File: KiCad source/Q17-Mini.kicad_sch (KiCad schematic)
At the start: 80 parts, among them J1 Input, J2-1 SPK+, J2-2 SPK-, J3-1 V+, J3-2 GND, J3-3 V-, Q1 IRF610, Q10 KSA992, Q11 BS250P, Q12 BD139, Q13 IRF610, Q14 IRF9610, Q15 FQA46N15, Q16 FQA36P15, Q2 KSA992, Q3 KSC1845, Q4 IRF9610, Q5 FQP3P20, Q6 FQP3N30, Q7 KSC1845, Q8 ZVN4206AV, Q9 BS250P, U1 OPA1641

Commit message: PCB v1.0.8 FINAL
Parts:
- R11, R12: value 47R/1W -> 47R/2W
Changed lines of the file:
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@@
   (title_block
     (title "Q17-Mini Amplifier")
-    (date "2021-11-27")
+    (date "2021-11-28")
     (rev "1.0.8")
     (company "by eng. Tiberiu Vicol")
@@
       (effects (font (size 1.27 1.27)) (justify left))
     )
-    (property "Value" "47R/1W" (id 1) (at 180.5941 69.9833 0)
+    (property "Value" "47R/2W" (id 1) (at 180.5941 69.9833 0)
       (effects (font (size 1.27 1.27)) (justify left))
     )
@@
       (effects (font (size 1.27 1.27)) (justify left))
     )
-    (property "Value" "47R/1W" (id 1) (at 180.5941 102.2413 0)
+    (property "Value" "47R/2W" (id 1) (at 180.5941 102.2413 0)
       (effects (font (size 1.27 1.27)) (justify left))
     )
@@
     )
     (path "/15b91c78-18e1-4f64-926c-7e4784683c4f"
-      (reference "R11") (unit 1) (value "47R/1W") (footprint "Resistor_THT:R_Axial_DIN0411_L9.9mm_D3.6mm_P12.70mm_Horizontal")
+      (reference "R11") (unit 1) (value "47R/2W") (footprint "Resistor_THT:R_Axial_DIN0411_L9.9mm_D3.6mm_P12.70mm_Horizontal")
     )
     (path "/650c038f-de6c-4533-9f4a-887a91a93957"
-      (reference "R12") (unit 1) (value "47R/1W") (footprint "Resistor_THT:R_Axial_DIN0411_L9.9mm_D3.6mm_P12.70mm_Horizontal")
+      (reference "R12") (unit 1) (value "47R/2W") (footprint "Resistor_THT:R_Axial_DIN0411_L9.9mm_D3.6mm_P12.70mm_Horizontal")
     )
     (path "/02f26f68-bf34-47b8-a58c-12fbe031c778"

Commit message: Schematic v1.0.9
Some mods on text.
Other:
- note added: "R27 : Use good low noise 1W resistor (CMF60560R00JKR6)."
- note removed: "R27 : Use good low noise and low ppm 1W resistor."
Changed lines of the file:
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@@
   (title_block
     (title "Q17-Mini Amplifier")
-    (date "2021-11-28")
-    (rev "1.0.8")
+    (date "2021-11-29")
+    (rev "1.0.9")
     (company "by eng. Tiberiu Vicol")
     (comment 1 "Modified by Stef for the Q17-Mini project")
@@
     (effects (font (size 1.27 1.27)) (justify left bottom))
   )
-  (text "R27 : Use good low noise and low ppm 1W resistor." (at 93.98 177.8 0)
+  (text "R27 : Use good low noise 1W resistor (CMF60560R00JKR6)."
+    (at 93.98 177.8 0)
     (effects (font (size 1.27 1.27)) (justify left bottom))
   )

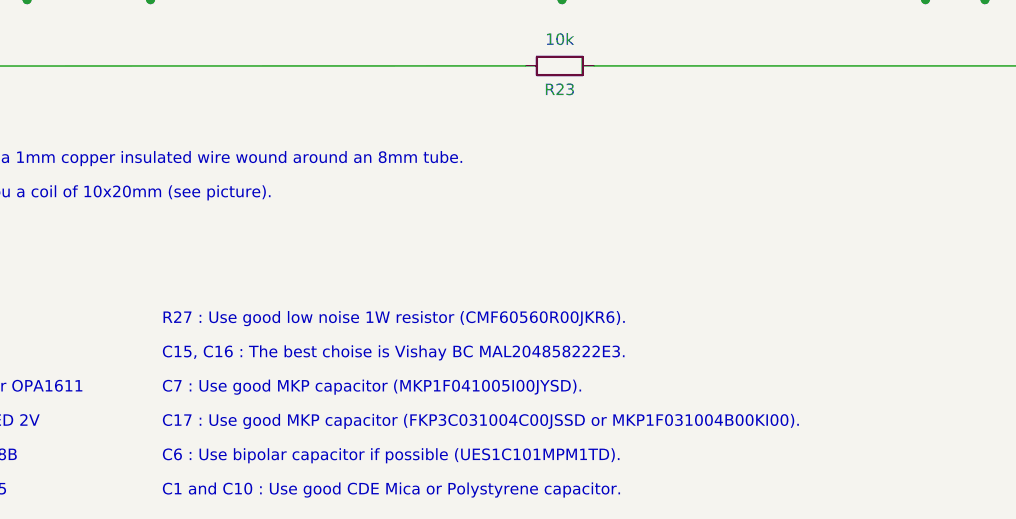
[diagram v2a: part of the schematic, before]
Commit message: Schematic v1.0.9
Some mods on comment text.
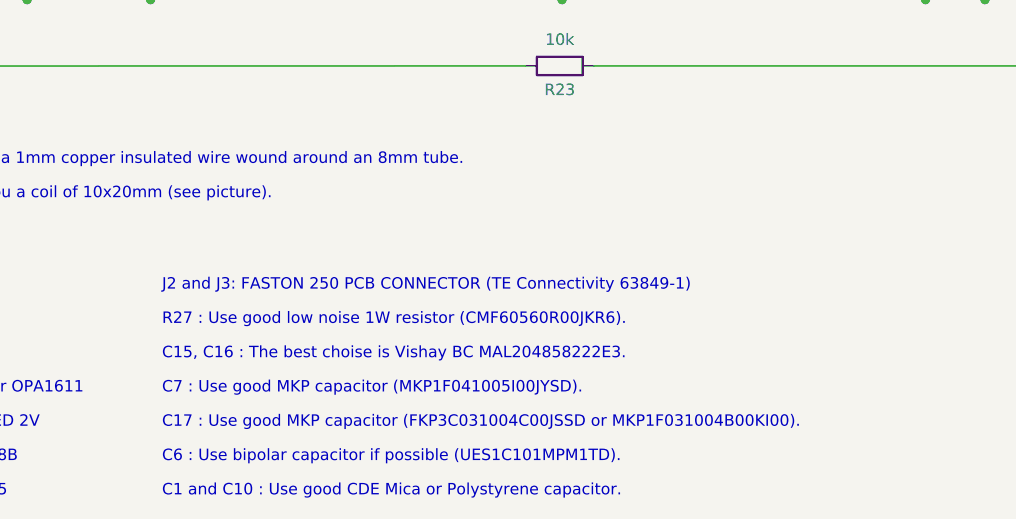
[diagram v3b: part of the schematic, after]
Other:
- note added: "J2 and J3: FASTON 250 PCB CONNECTOR (TE Connectivity 63849-1)"
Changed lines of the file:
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@@
+    (effects (font (size 1.27 1.27)) (justify left bottom))
+  )
+  (text "J2 and J3: FASTON 250 PCB CONNECTOR (TE Connectivity 63849-1)"
+    (at 93.98 173.99 0)
     (effects (font (size 1.27 1.27)) (justify left bottom))
   )

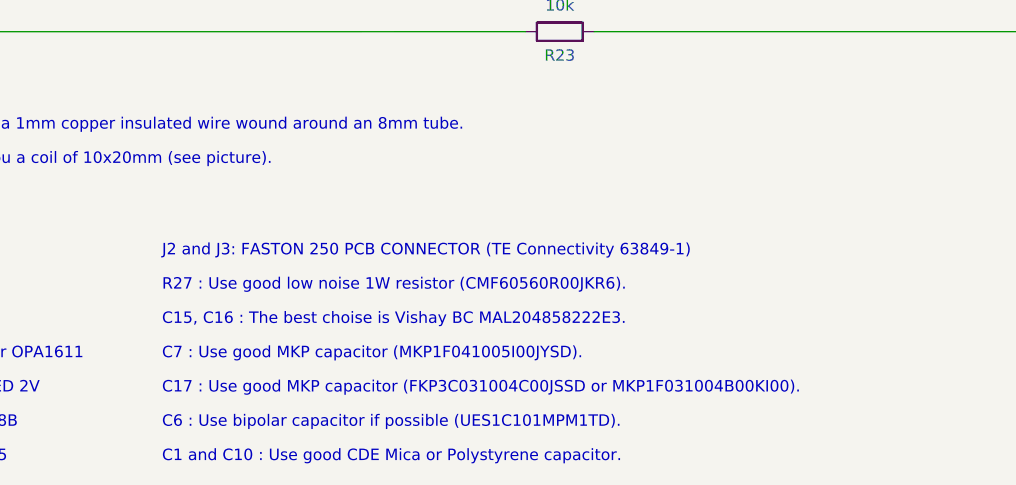
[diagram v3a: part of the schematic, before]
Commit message: Schematic v1.0.9
Added references for capacitors.
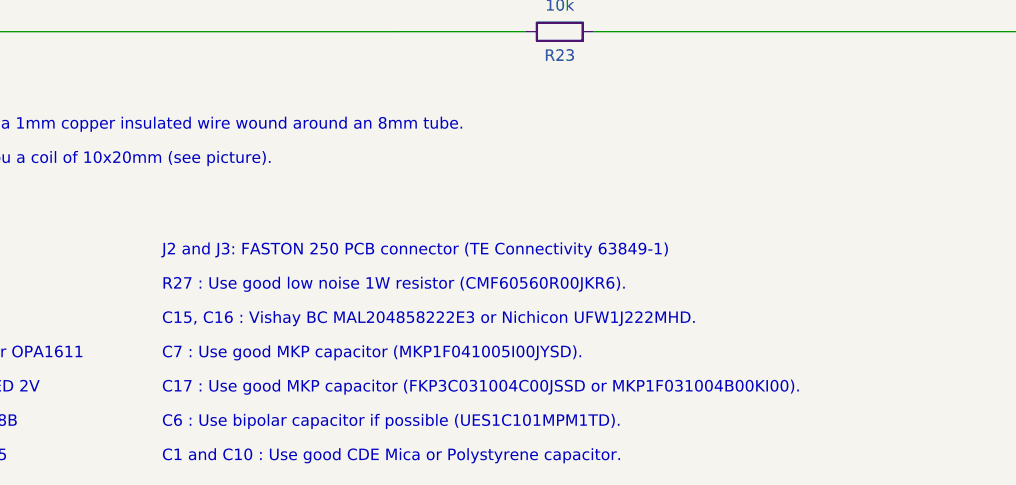
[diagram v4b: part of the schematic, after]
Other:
- note added: "C15, C16 : Vishay BC MAL204858222E3 or Nichicon UFW1J222MHD."
- note added: "J2 and J3: FASTON 250 PCB connector (TE Connectivity 63849-1)"
- note removed: "C15, C16 : The best choise is Vishay BC MAL204858222E3."
- note removed: "J2 and J3: FASTON 250 PCB CONNECTOR (TE Connectivity 63849-1)"
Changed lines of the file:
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@@
     (effects (font (size 1.27 1.27)) (justify left bottom))
   )
-  (text "J2 and J3: FASTON 250 PCB CONNECTOR (TE Connectivity 63849-1)"
+  (text "J2 and J3: FASTON 250 PCB connector (TE Connectivity 63849-1)"
     (at 93.98 173.99 0)
     (effects (font (size 1.27 1.27)) (justify left bottom))
@@
     (effects (font (size 1.27 1.27)) (justify left bottom))
   )
-  (text "C15, C16 : The best choise is Vishay BC MAL204858222E3."
+  (text "C15, C16 : Vishay BC MAL204858222E3 or Nichicon UFW1J222MHD."
     (at 93.98 181.61 0)
     (effects (font (size 1.27 1.27)) (justify left bottom))

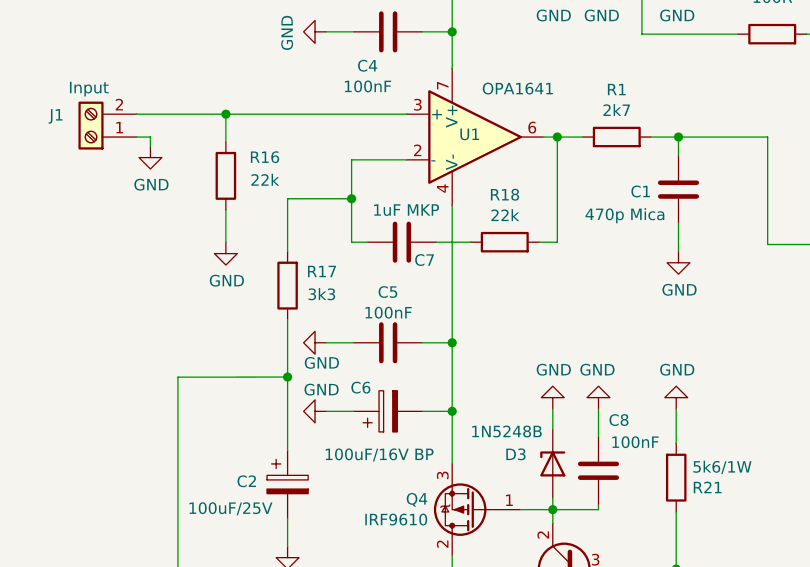
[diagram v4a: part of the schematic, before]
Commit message: Schematic 1.0.9
Update C7 footprint (Pin 1 and 2 inverted).
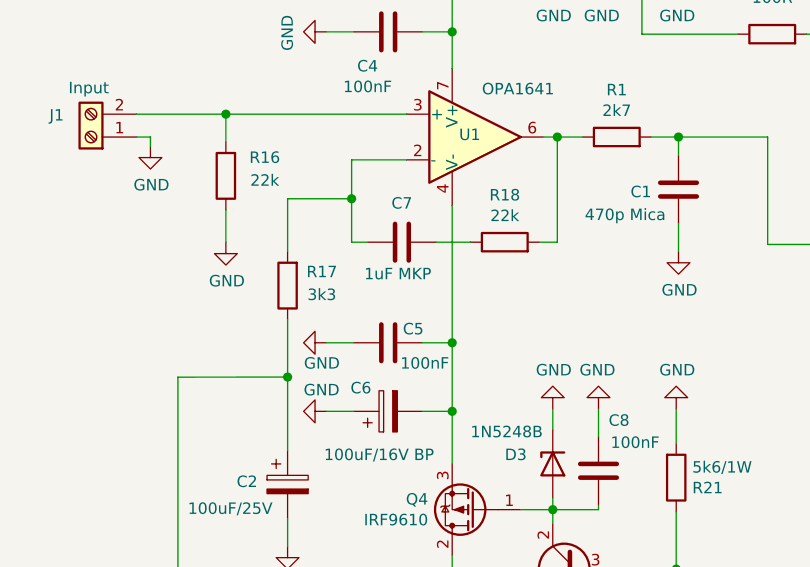
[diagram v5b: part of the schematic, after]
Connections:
- net at C7.1: now also R17.2, U1.2 (-); no longer R18.1
- new net: C7.2, R18.1
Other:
- moved on the sheet: C7
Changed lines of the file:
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@@
   (title_block
     (title "Q17-Mini Amplifier")
-    (date "2021-11-29")
+    (date "2021-11-30")
     (rev "1.0.9")
     (company "by eng. Tiberiu Vicol")
@@
     (pin "3")
   )
-  (symbol (lib_id "Device:C") (at 62.23 88.138 270) (unit 1)
-    (in_bom yes) (on_board yes)
-    (property "Reference" "C7" (id 0) (at 64.77 90.17 90))
-    (property "Value" "1uF MKP" (id 1) (at 62.6845 84.6078 90))
-    (property "Footprint" "Capacitor_THT:C_Rect_C7_Q17-Mini" (id 2) (at 58.42 89.1032 0)
+  (symbol (lib_name "C_1") (lib_id "Device:C") (at 62.23 88.138 90) (unit 1)
+    (in_bom yes) (on_board yes)
+    (property "Reference" "C7" (id 0) (at 62.23 83.82 90))
+    (property "Value" "1uF MKP" (id 1) (at 61.7755 91.6682 90))
+    (property "Footprint" "Capacitor_THT:C_Rect_C7_Q17-Mini" (id 2) (at 66.04 87.1728 0)
       (effects (font (size 1.27 1.27)) hide)
     )
@@
     (pin "3")
   )
-  (symbol (lib_id "Device:R") (at 73.66 88.138 90) (unit 1)
+  (symbol (lib_name "R_1") (lib_id "Device:R") (at 73.66 88.138 90) (unit 1)
     (in_bom yes) (on_board yes)
     (property "Reference" "R18" (id 0) (at 73.66 82.9118 90))
@@
   (symbol (lib_id "Device:C") (at 60.706 99.314 90) (unit 1)
     (in_bom yes) (on_board yes)
-    (property "Reference" "C5" (id 0) (at 60.706 93.7218 90))
-    (property "Value" "100nF" (id 1) (at 60.706 96.0205 90))
+    (property "Reference" "C5" (id 0) (at 63.5 97.79 90))
+    (property "Value" "100nF" (id 1) (at 64.77 101.6 90))
     (property "Footprint" "Capacitor_THT:C_Rect_L7.2mm_W2.5mm_P5.00mm_FKS2_FKP2_MKS2_MKP2" (id 2) (at 64.516 98.3488 0)
       (effects (font (size 1.27 1.27)) hide)

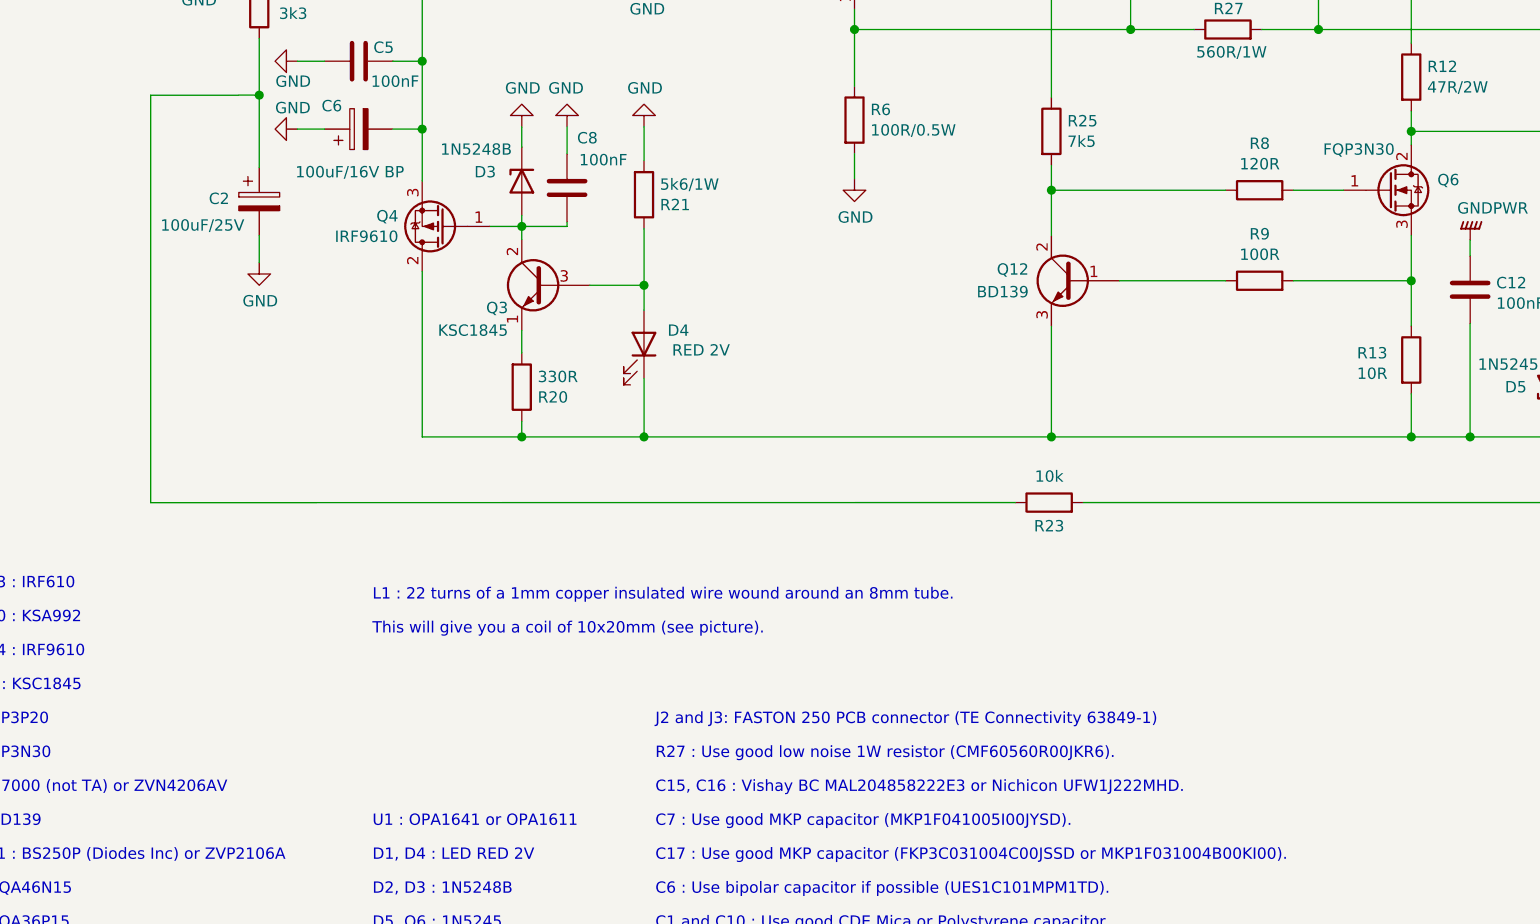
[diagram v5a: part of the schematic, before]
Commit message: Schematic v1.1.0 and PCB v1.0.9
- Corrected error for C2/C6. C2 is the BP capacitor not C6.
- Changed silkscreen for C2/C6 on PCB.
- New Q17-Mini-BOM and 3D pictures.
- Inverted C1 to have the GND at the right place on the PCB.
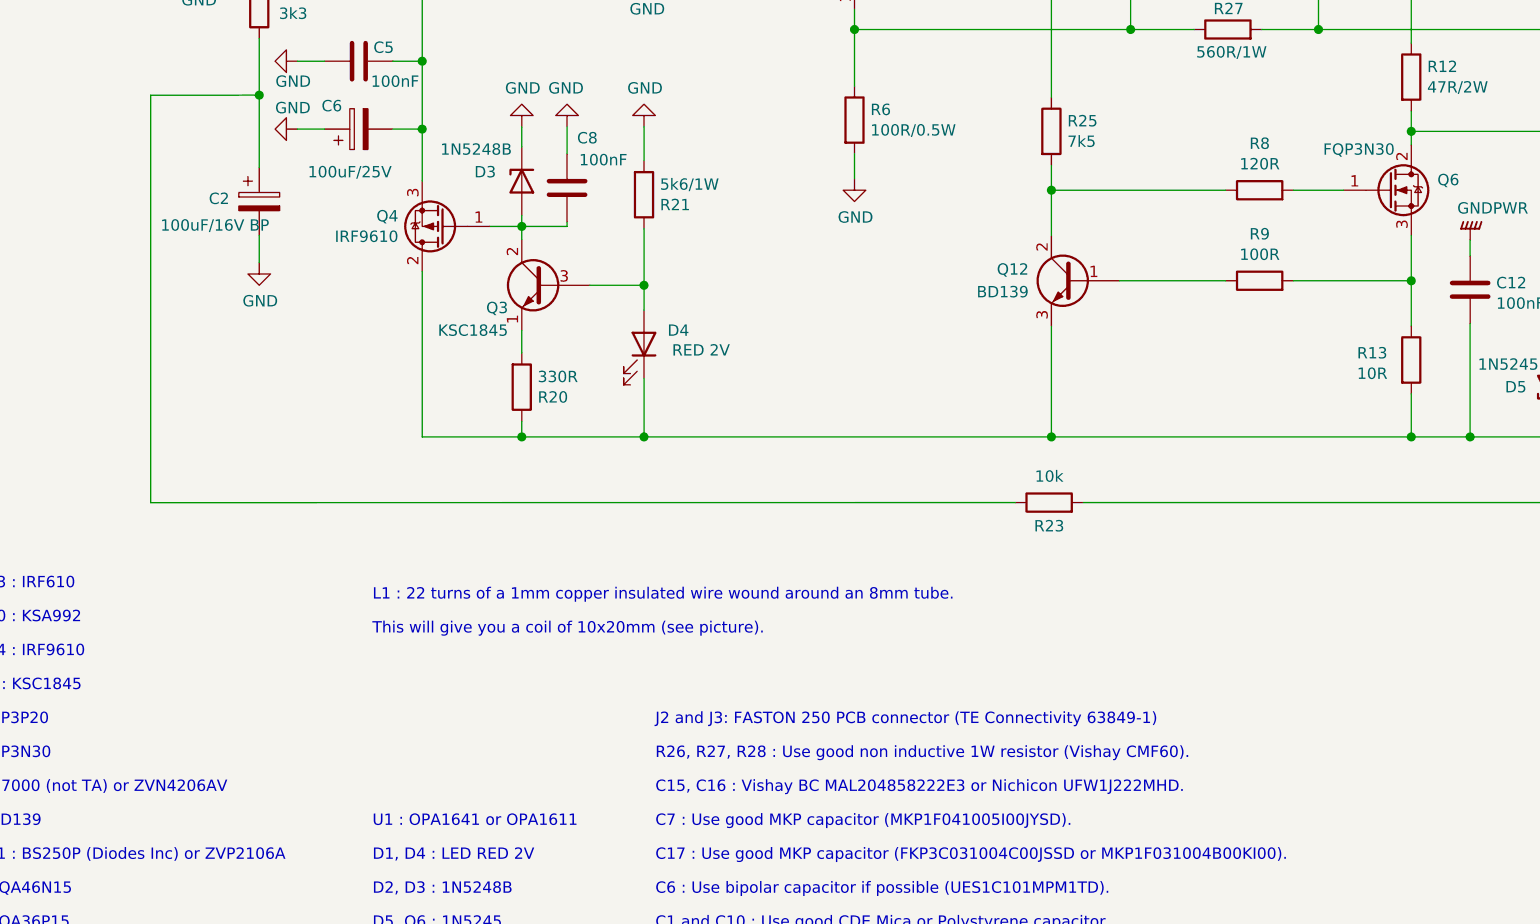
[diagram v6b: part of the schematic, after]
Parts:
- C2: value 100uF/25V -> 100uF/16V BP
- C6: value 100uF/16V BP -> 100uF/25V
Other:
- note added: "R26, R27, R28 : Use good non inductive 1W resistor (Vishay CMF60)."
- note removed: "R27 : Use good low noise 1W resistor (CMF60560R00JKR6)."
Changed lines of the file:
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@@
     (title "Q17-Mini Amplifier")
     (date "2021-11-30")
-    (rev "1.0.9")
+    (rev "1.1.0")
     (company "by eng. Tiberiu Vicol")
     (comment 1 "Modified by Stef for the Q17-Mini project")
@@
     (effects (font (size 1.27 1.27)) (justify left bottom))
   )
-  (text "R27 : Use good low noise 1W resistor (CMF60560R00JKR6)."
+  (text "R26, R27, R28 : Use good non inductive 1W resistor (Vishay CMF60)."
     (at 93.98 177.8 0)
     (effects (font (size 1.27 1.27)) (justify left bottom))
@@
     (in_bom yes) (on_board yes)
     (property "Reference" "C6" (id 0) (at 57.6781 104.347 90))
-    (property "Value" "100uF/16V BP" (id 1) (at 59.69 111.76 90))
+    (property "Value" "100uF/25V" (id 1) (at 59.69 111.76 90))
     (property "Footprint" "Capacitor_THT:CP_Radial_D10.0mm_P5.00mm" (id 2) (at 64.516 105.9688 0)
       (effects (font (size 1.27 1.27)) hide)
@@
       (effects (font (size 1.27 1.27)) (justify left))
     )
-    (property "Value" "100uF/25V" (id 1) (at 38.4365 117.74 0)
+    (property "Value" "100uF/16V BP" (id 1) (at 38.4365 117.74 0)
       (effects (font (size 1.27 1.27)) (justify left))
     )
@@
     )
     (path "/61bf8854-9a50-4642-8024-43beb183f09b"
-      (reference "C2") (unit 1) (value "100uF/25V") (footprint "Capacitor_THT:CP_Radial_D10.0mm_P5.00mm")
+      (reference "C2") (unit 1) (value "100uF/16V BP") (footprint "Capacitor_THT:CP_Radial_D10.0mm_P5.00mm")
     )
     (path "/f9e8c33b-6fda-41be-bb30-ce5c13715e36"
@@
     )
     (path "/553e7843-c1ff-4dc6-ae3e-d89ae303f31a"
-      (reference "C6") (unit 1) (value "100uF/16V BP") (footprint "Capacitor_THT:CP_Radial_D10.0mm_P5.00mm")
+      (reference "C6") (unit 1) (value "100uF/25V") (footprint "Capacitor_THT:CP_Radial_D10.0mm_P5.00mm")
     )
     (path "/54c34d9c-31cf-4362-89c6-22284b93a5d2"

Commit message: Parts changes for C2.
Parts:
- C3, C6: value 100uF/25V -> 100uF/16V
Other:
- note added: "C2 : Use bipolar capacitor if possible (Nichicon Muse UES1A101MPM)."
- note removed: "C6 : Use bipolar capacitor if possible (UES1C101MPM1TD)."
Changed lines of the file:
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@@
     (effects (font (size 1.27 1.27)) (justify left bottom))
   )
-  (text "C6 : Use bipolar capacitor if possible (UES1C101MPM1TD)."
+  (text "C2 : Use bipolar capacitor if possible (Nichicon Muse UES1A101MPM)."
     (at 93.98 193.04 0)
     (effects (font (size 1.27 1.27)) (justify left bottom))
@@
     (in_bom yes) (on_board yes)
     (property "Reference" "C6" (id 0) (at 57.6781 104.347 90))
-    (property "Value" "100uF/25V" (id 1) (at 59.69 111.76 90))
+    (property "Value" "100uF/16V" (id 1) (at 59.69 111.76 90))
     (property "Footprint" "Capacitor_THT:CP_Radial_D10.0mm_P5.00mm" (id 2) (at 64.516 105.9688 0)
       (effects (font (size 1.27 1.27)) hide)
@@
     (in_bom yes) (on_board yes)
     (property "Reference" "C3" (id 0) (at 60.96 50.8 90))
-    (property "Value" "100uF/25V" (id 1) (at 60.96 53.0987 90))
+    (property "Value" "100uF/16V" (id 1) (at 60.96 53.0987 90))
     (property "Footprint" "Capacitor_THT:CP_Radial_D10.0mm_P5.00mm" (id 2) (at 56.896 58.1152 0)
       (effects (font (size 1.27 1.27)) hide)
@@
     )
     (path "/f9e8c33b-6fda-41be-bb30-ce5c13715e36"
-      (reference "C3") (unit 1) (value "100uF/25V") (footprint "Capacitor_THT:CP_Radial_D10.0mm_P5.00mm")
+      (reference "C3") (unit 1) (value "100uF/16V") (footprint "Capacitor_THT:CP_Radial_D10.0mm_P5.00mm")
     )
     (path "/0c730a87-391f-4174-a498-479612b6c1cd"
@@
     )
     (path "/553e7843-c1ff-4dc6-ae3e-d89ae303f31a"
-      (reference "C6") (unit 1) (value "100uF/25V") (footprint "Capacitor_THT:CP_Radial_D10.0mm_P5.00mm")
+      (reference "C6") (unit 1) (value "100uF/16V") (footprint "Capacitor_THT:CP_Radial_D10.0mm_P5.00mm")
     )
     (path "/54c34d9c-31cf-4362-89c6-22284b93a5d2"
